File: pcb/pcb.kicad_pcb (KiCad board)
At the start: 2 copper layers, 91.6 x 74.2 mm, 42 parts, among them J0 P_motors, J1 L_motors, J2 R_motors, J3 RPi, J4 AVR-ISP-6, J5 Sensor_0, J6 Sensor_1, J7 Vin, U0 DRV8848, U1 DRV8848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

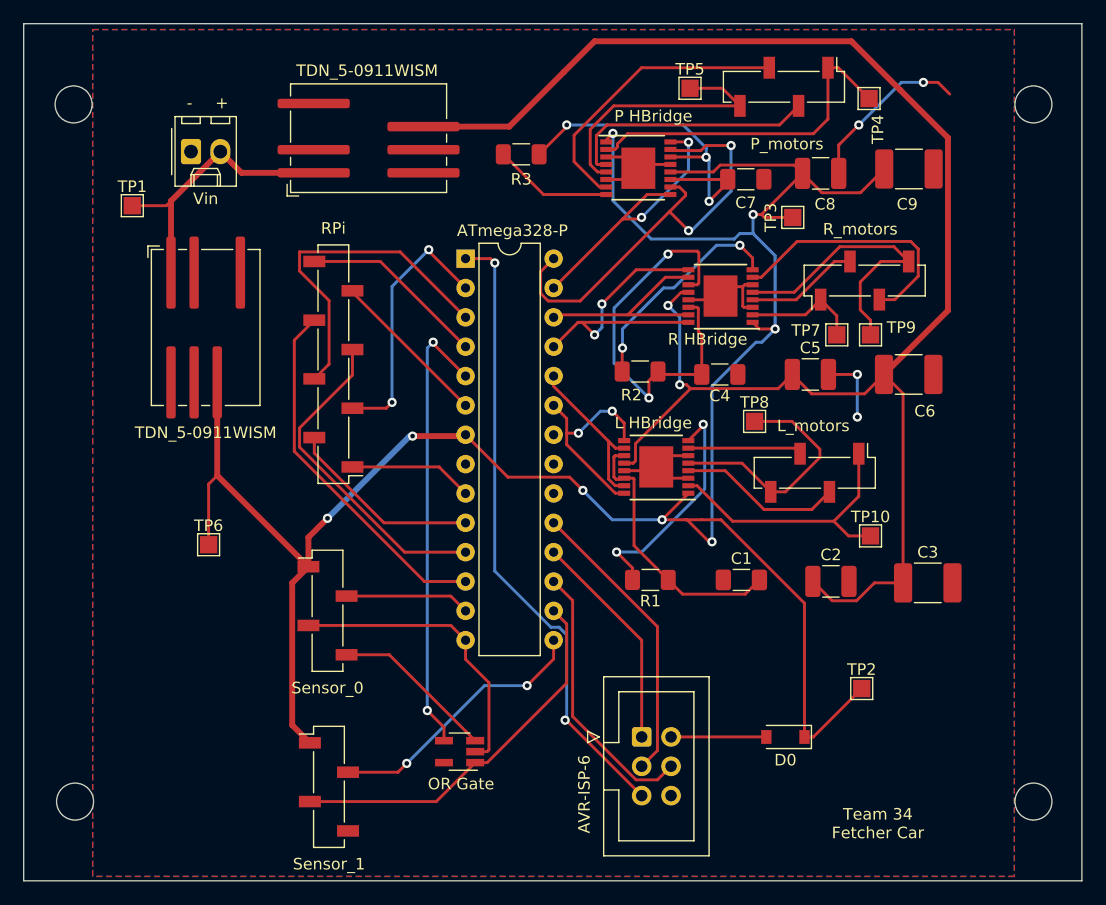
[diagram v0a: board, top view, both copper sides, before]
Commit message: Adding the final version of the PCB blueprint
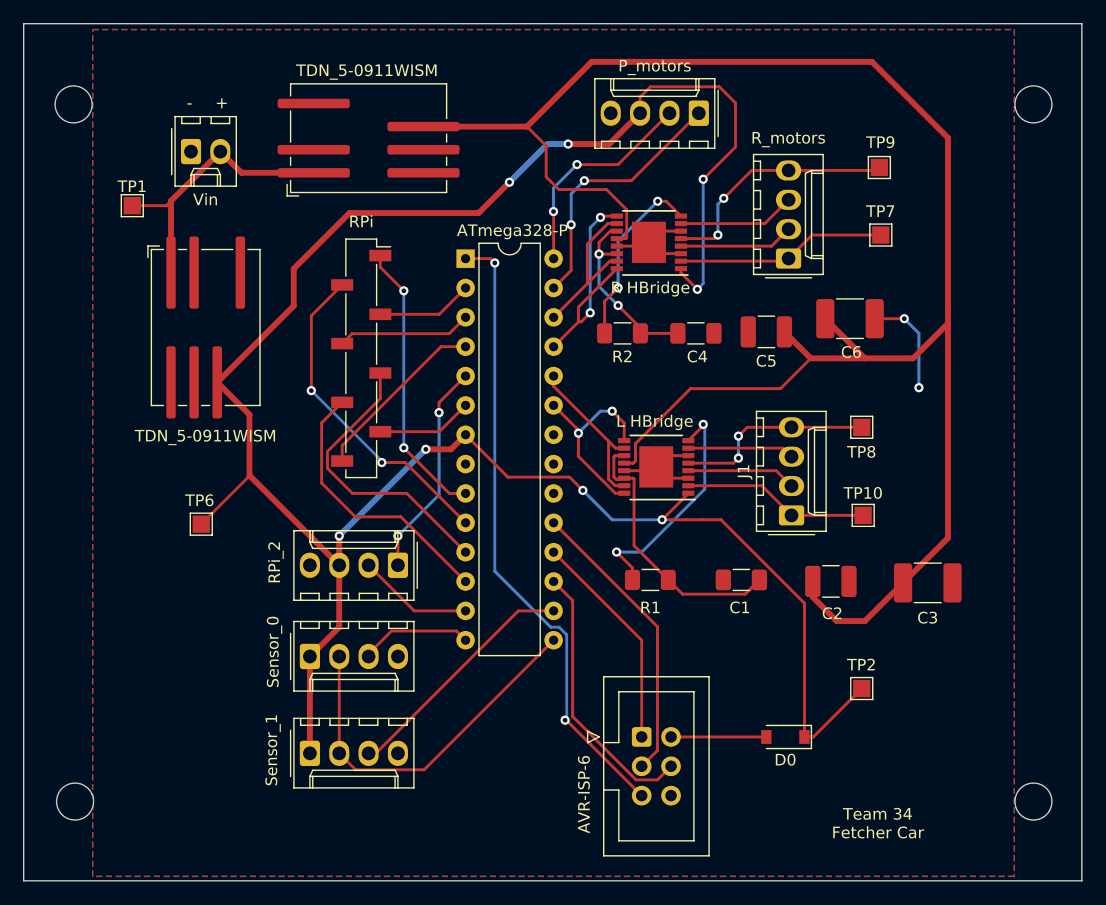
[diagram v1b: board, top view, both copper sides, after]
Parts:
- removed C7: 2.2uF, Capacitor_SMD:C_1206_3216Metric_Pad1.33x1.80mm_HandSolder
- removed C8: 10uF, Capacitor_SMD:C_1210_3225Metric_Pad1.33x2.70mm_HandSolder
- removed C9: 0.1uF, Capacitor_SMD:C_1812_4532Metric_Pad1.57x3.40mm_HandSolder
- removed J0: P_motors, Connector_PinSocket_2.54mm:PinSocket_1x04_P2.54mm_Vertical_SMD_Pin1Left
- removed R3: 5k, Resistor_SMD:R_1206_3216Metric_Pad1.30x1.75mm_HandSolder
- removed TP3, TP4, TP5: TestPoint, TestPoint:TestPoint_Pad_1.5x1.5mm
- removed U0: DRV8848, Package_SO:TSSOP-16-1EP_4.4x5mm_P0.65mm
- removed U4: 74AHC1G32, Package_TO_SOT_SMD:SOT-23-5_HandSoldering
- added J8: P_motors, Connector_Molex:Molex_KK-254_AE-6410-04A_1x04_P2.54mm_Vertical, F.Cu at (160.4, 42.2)
- added J9: RPi_2, Connector_Molex:Molex_KK-254_AE-6410-04A_1x04_P2.54mm_Vertical, F.Cu at (134.4, 81.3)
- J1, J2, J5, J6: footprint Connector_PinSocket_2.54mm:PinSocket_1x04_P2.54mm_Vertical_SMD_Pin1Left -> Connector_Molex:Molex_KK-254_AE-6410-04A_1x04_P2.54mm_Vertical
- J3: footprint Connector_PinSocket_2.54mm:PinSocket_1x08_P2.54mm_Vertical_SMD_Pin1Left -> Connector_PinSocket_2.54mm:PinSocket_1x08_P2.54mm_Vertical_SMD_Pin1Right
- moved TP9 14.5 mm to (176.0, 46.9)
- moved TP7 9.44 mm to (176.1, 52.7)
- moved TP8 9.28 mm to (174.5, 69.3)
- moved U2 7.74 mm to (156.1, 53.3)
- moved C6 7.01 mm to (173.5, 59.9)
- moved J2 6.85 mm to (168.2, 54.7)
- moved C5 5.30 mm to (166.2, 61.1), turned to 180 degrees
- moved J5 4.24 mm to (126.7, 89.2)
- moved J1 4.20 mm to (168.4, 77.0), turned to 90 degrees
- moved C4 4.11 mm to (160.1, 61.2)
- moved R2 3.64 mm to (153.8, 61.2)
- moved J6 3.34 mm to (126.7, 97.6)
- moved J3 2.47 mm to (131.2, 63.4), turned to 0 degrees
- moved TP6 1.89 mm to (117.3, 77.7)
- moved TP10 1.89 mm to (174.6, 77.0)
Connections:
- J6 pad 2: /TRIG_1 -> /TRIG_0
- U3 pad 13: /TRIG_0 -> /Proximity_Data
- U3 pad 15: /TRIG_1 -> /TRIG_0
- U3 pad 5: /Sensor_INT -> /CTRL_ACK
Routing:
- net /Sensor_INT: track 39.4 -> 0.00 mm, vias 2 -> 0
- net GND: track 55.0 -> 22.1 mm, vias 4 -> 2
- net /VINT3: track 31.8 -> 0.00 mm, vias 3 -> 0
- net Net-(J0-Pad1): track 29.5 -> 0.00 mm
- net Net-(J0-Pad3): track 25.3 -> 0.00 mm
- net /TRIG_1: track 23.5 -> 0.00 mm, vias 2 -> 0
- net Net-(J0-Pad4): track 23.4 -> 0.00 mm
- net Net-(J0-Pad2): track 21.9 -> 0.00 mm
- net /TRIG_0: track 10.8 -> 32.2 mm
- net /Pincers_out1: track 38.7 -> 18.8 mm
- net +5VA: track 141.1 -> 160.4 mm, vias 2 -> 0
- net /VINT2: track 35.3 -> 16.1 mm
- net /CTRL_ACK: track 0.00 -> 18.8 mm, vias 0 -> 2
- net /Rmotors_in1: track 29.3 -> 11.6 mm
- net /ECHO_0: track 25.7 -> 9.77 mm
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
